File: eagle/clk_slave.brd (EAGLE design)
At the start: 31.8 x 19.1 mm, 31 parts, among them U1 SIT3808AI-22-33NB-25.000000Y, U2 74LVCU04A, U3 74LVC86A, U4 74LVC74A

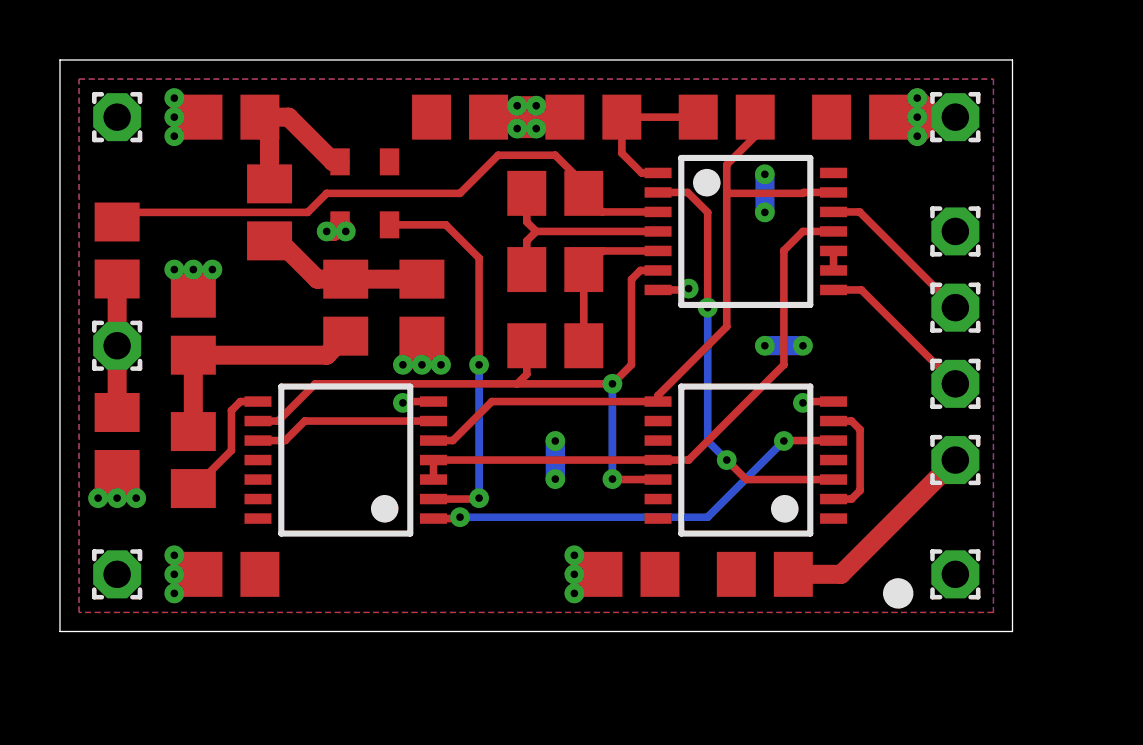
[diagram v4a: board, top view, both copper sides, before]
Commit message: fix slave clock board layout
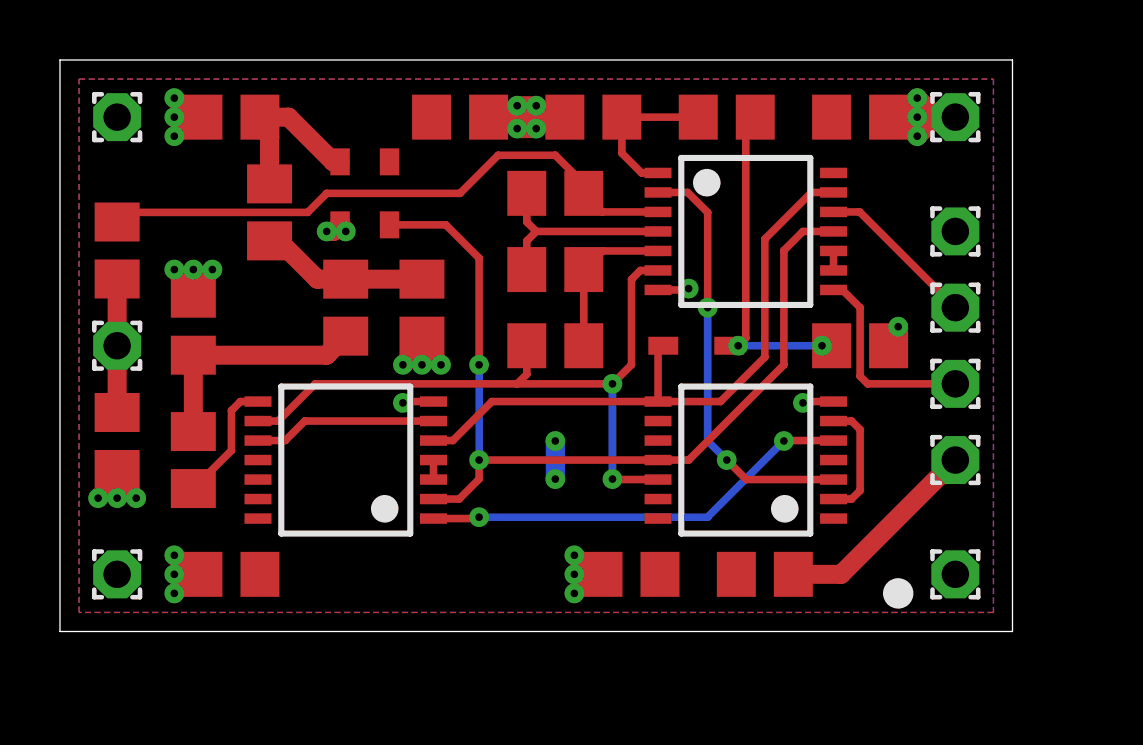
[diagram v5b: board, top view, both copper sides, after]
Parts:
- added D1: MMDL914T1G, ref-packages:SOD323
- added R8: 47k, ref-packages:R0805
- C2: value 1u -> 100n
- C3: value 330n -> 100n
- R2: value 330 -> 3.3k
- R3: value 100 -> 1k
- R4: value 33 -> 330
- R5: value 47k -> 1k
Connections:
- net SRC renamed REF
- removed net ALIGN: R4.1, U3.8
- new net FILT3: C2.1, R2.1, U1.1
- new net TIMER: D1.1, R5.1, R8.2
- net !PPS: now also D1.2; no longer R5.1
- net FB: now also R4.1, U3.8; no longer C2.1, R2.1, U1.1
- net GND: now also R8.1
- net OCLK: no longer U2.11, U4.11
- net OSC: now also U2.11, U4.11
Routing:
- net OCLK: track 19.4 -> 0.65 mm
- net OSC: track 13.0 -> 29.8 mm
- net TIMER: track 0.00 -> 11.3 mm, vias 0 -> 2
- net FILT3: track 0.00 -> 5.64 mm
- net ALIGN: track 4.14 -> 0.00 mm
- net V3.3: track 3.81 -> 1.27 mm, vias 6 -> 2
- net FB: track 5.64 -> 4.14 mm
- net !PPS: track 22.4 -> 21.0 mm
- net CLK: track 5.36 -> 6.70 mm
- net GND: track 35.6 -> 36.4 mm, vias 30 -> 31
